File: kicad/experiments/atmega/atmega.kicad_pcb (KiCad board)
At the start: 2 copper layers, 8 parts, among them IC1 ATMEGA328P-A, P1 ISCP, P2 SERIAL, P3 CONN_01X05

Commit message: Layout
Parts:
- added C3: 0.1uF, Capacitors_SMD:C_0805_HandSoldering, F.Cu at (152.0, 94.7)
- added P4: GPIO, theapi:SMD_Header_Straight_1x05, B.Cu at (140.2, 106.2)
- added R2: 10k, Resistors_SMD:R_0805_HandSoldering, B.Cu at (142.8, 111.7)
- P2: value SERIAL -> FTDI; footprint Pin_Headers:Pin_Header_Straight_1x03 -> Socket_Strips:Socket_Strip_Straight_1x06
- P3: value CONN_01X05 -> I2C; footprint Pin_Headers:Pin_Header_Straight_1x05 -> SMD_Header_Straight_1x05; moved to B.Cu
- moved D1 75.0 mm to (142.2, 111.3), turned to 180 degrees
- moved C2 64.1 mm to (139.3, 96.6), turned to 90 degrees
- moved P3 63.2 mm to (152.0, 95.9), turned to 180 degrees
- moved P2 62.9 mm to (139.7, 92.5), turned to 0 degrees
- moved R1 61.3 mm to (142.7, 108.7)
- moved IC1 59.7 mm to (146.1, 101.6)
- moved C1 55.8 mm to (139.3, 101.7), turned to 270 degrees
- moved P1 45.8 mm to (152.4, 111.8), turned to 180 degrees
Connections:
- P1 pad 3: /CLK -> /SCK
- P2 pad 2: /TX -> GND
- P2 pad 3: /RX -> +3V3
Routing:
- net GND: track 0.00 -> 64.9 mm, vias 0 -> 1
- net +3V3: track 0.00 -> 57.8 mm, vias 0 -> 1
- net /RESET: track 0.00 -> 36.6 mm
- net /INT0: track 0.00 -> 13.9 mm, vias 0 -> 1
- net /SCK: track 0.00 -> 12.4 mm, vias 0 -> 1
- net /PD6: track 0.00 -> 10.9 mm, vias 0 -> 1
- net /PB2/SS: track 0.00 -> 8.99 mm, vias 0 -> 1
- net /SDA: track 0.00 -> 8.88 mm, vias 0 -> 1
- net /MISO: track 0.00 -> 8.74 mm
- net /SCL: track 0.00 -> 8.53 mm, vias 0 -> 1
- net /PB1: track 0.00 -> 8.19 mm, vias 0 -> 1
- net /PD5: track 0.00 -> 8.10 mm, vias 0 -> 1
- net /PD3: track 0.00 -> 7.92 mm, vias 0 -> 1
- net /RX: track 0.00 -> 7.92 mm
- net /TX: track 0.00 -> 6.72 mm
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- added copper zone on B.Cu, net GND
- added copper zone on F.Cu, net GND
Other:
- board outline added: 16.8 x 23.4 mm
- net class Default: clearance 0.1524 -> 0.2032; trace_width 0.1524 -> 0.2032
- rule trace_clearance: 0.1524 -> 0.2032
- rule trace_min: 0.1524 -> 0.2032

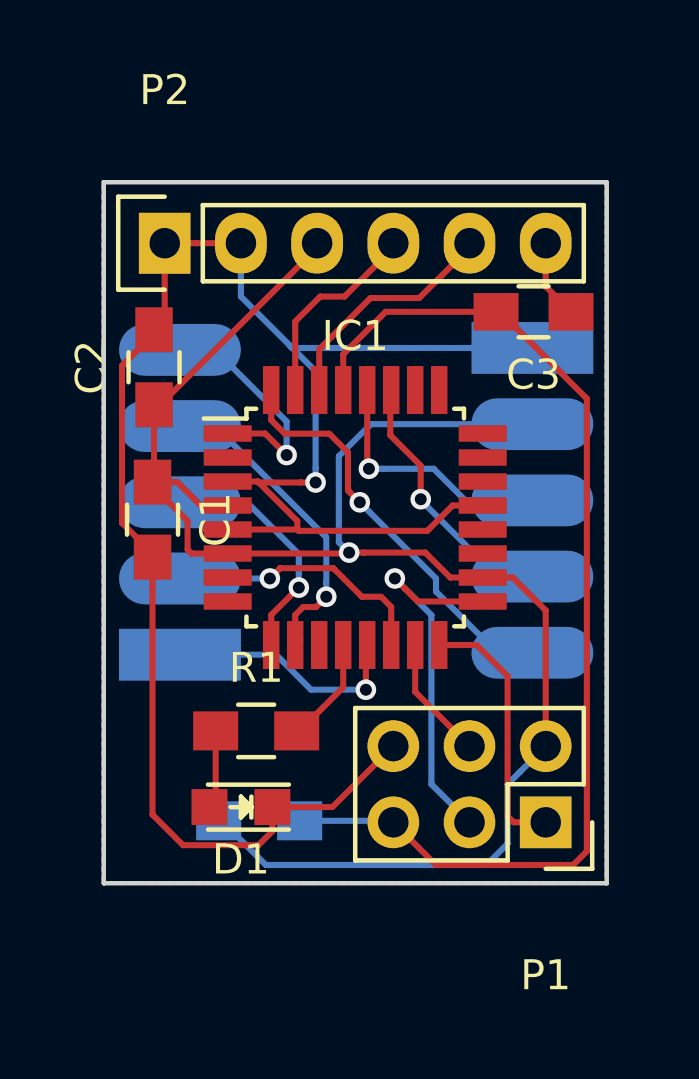
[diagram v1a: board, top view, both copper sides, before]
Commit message: Through hole headers
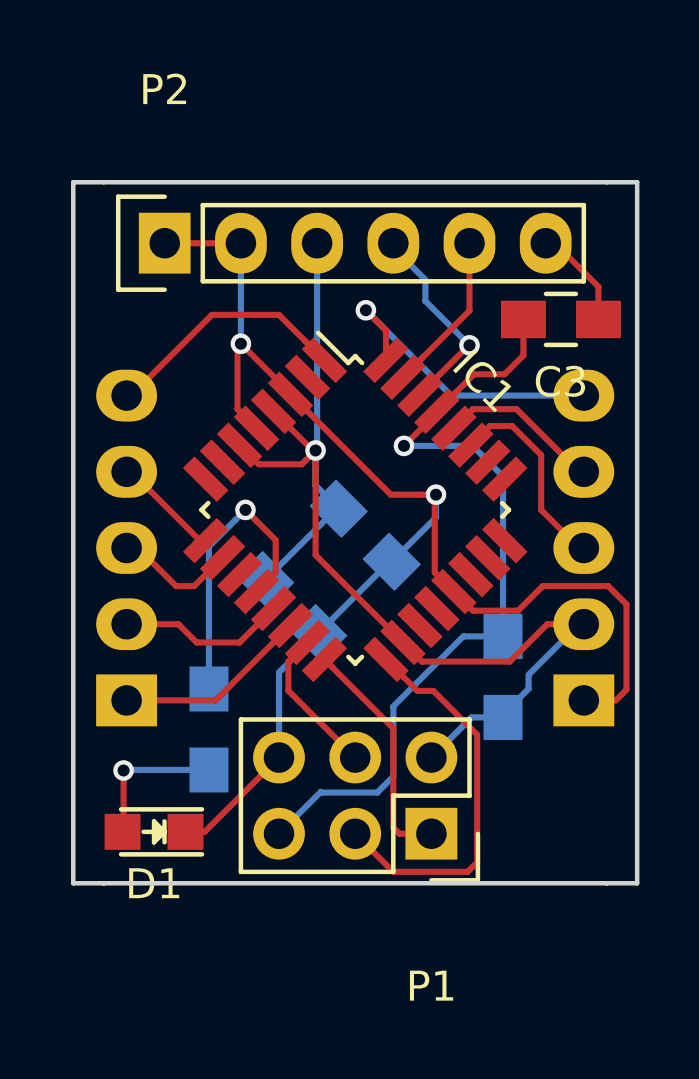
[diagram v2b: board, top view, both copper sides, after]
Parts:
- C1, C2, R1: moved to B.Cu
- P3: footprint SMD_Header_Straight_1x05 -> Pin_Headers:Pin_Header_Straight_1x05
- P4: footprint theapi:SMD_Header_Straight_1x05 -> Pin_Headers:Pin_Header_Straight_1x05
- moved P3 11.9 mm to (153.7, 107.7), turned to 0 degrees
- moved R2 9.44 mm to (151.0, 106.9), turned to 90 degrees
- moved C2 9.20 mm to (143.9, 104.6), turned to 315 degrees
- moved C1 7.11 mm to (146.4, 102.2), turned to 315 degrees
- moved P1 3.83 mm to (148.6, 112.1)
- moved D1 3.01 mm to (139.3, 112.1)
- moved P4 2.34 mm to (138.4, 107.7)
- moved R1 1.58 mm to (141.2, 108.7), turned to 90 degrees
- moved C3 0.95 mm to (152.9, 95.0)
- moved IC1 0.25 mm to (146.1, 101.3), turned to 315 degrees
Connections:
- P2 pad 4: /TX -> /RX
- P2 pad 5: /RX -> /TX
- P3 pad 3: /SCL -> /SDA
- P3 pad 4: /SDA -> /SCL
- P4 pad 1: /PB1 -> /PB2/SS
- P4 pad 2: /PB2/SS -> /PB1
- P4 pad 3: /PD5 -> /PD6
- P4 pad 4: /PD6 -> /PD5
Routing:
- net +3V3: track 57.8 -> 39.3 mm
- net GND: track 64.9 -> 47.8 mm, vias 1 -> 2
- net (no net): track 0.00 -> 15.2 mm
- net /RESET: track 36.6 -> 27.3 mm, vias 0 -> 1
- net /PD6: track 10.9 -> 4.12 mm, vias 1 -> 0
- net /PB0: track 3.56 -> 9.87 mm, vias 0 -> 1
- net /PD5: track 8.10 -> 3.59 mm, vias 1 -> 0
- net /INT0: track 13.9 -> 10.4 mm
- net /SCL: track 8.53 -> 5.46 mm, vias 1 -> 0
- net /PB2/SS: track 8.99 -> 6.50 mm, vias 1 -> 0
- net /PB1: track 8.19 -> 5.77 mm, vias 1 -> 0
- net Net-(D1-Pad2): track 2.63 -> 4.91 mm, vias 0 -> 1
- net /SDA: track 8.88 -> 6.78 mm, vias 1 -> 0
- net /TX: track 6.72 -> 5.54 mm
- net /RX: track 7.92 -> 6.94 mm, vias 0 -> 1
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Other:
- board size 16.8 x 23.4 mm -> 18.8 x 23.4 mm

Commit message: Silkscreen
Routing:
- net (no net): track 15.2 -> 0.00 mm
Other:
- board text added: "."
- board text added: "2"
- board text added: "3"
- board text added: "3V3"
- board text added: "5"
- board text added: "6"
- board text added: "9"
- board text added: "A4"
- board text added: "A5"
- board text added: "DTR"
- board text added: "GND"
- board text added: "RX"
- board text added: "TX"
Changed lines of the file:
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@@
     (area 136.576999 90.348999 155.523001 113.867001)
     (thickness 1.6)
-    (drawings 9)
-    (tracks 165)
+    (drawings 24)
+    (tracks 164)
     (zones 0)
     (modules 11)
@@
     (aux_axis_origin 0 0)
     (grid_origin 139.7 92.456)
-    (visible_elements 7FFFFFFF)
+    (visible_elements 7FFFFF7F)
     (pcbplotparams
       (layerselection 0x010f0_80000001)
@@
     (tags "capacitor 0805")
     (attr smd)
-    (fp_text reference C2 (at 0 2.1 315) (layer B.SilkS)
-      (effects (font (size 1 1) (thickness 0.15)) (justify mirror))
-    )
-    (fp_text value 10uF (at 0 -2.1 315) (layer B.Fab)
-      (effects (font (size 1 1) (thickness 0.15)) (justify mirror))
+    (fp_text reference C2 (at 0.007237 1.76013 315) (layer B.SilkS)
+      (effects (font (size 1.016 1.016) (thickness 0.1524)) (justify mirror))
+    )
+    (fp_text value 10uF (at 0 -2.1 315) (layer B.SilkS) hide
+      (effects (font (size 1.016 1.016) (thickness 0.1524)) (justify mirror))
     )
     (fp_line (start -2.3 1) (end 2.3 1) (layer B.CrtYd) (width 0.05))
@@
     (tags "QFP 0.8")
     (attr smd)
-    (fp_text reference IC1 (at 0 -6.05 315) (layer F.SilkS)
-      (effects (font (size 1 1) (thickness 0.15)))
-    )
-    (fp_text value ATMEGA328P-A (at 0 6.05 315) (layer F.Fab)
+    (fp_text reference IC1 (at 0 -6.05 315) (layer F.SilkS) hide
+      (effects (font (size 1 1) (thickness 0.15)))
+    )
+    (fp_text value ATMEGA328P-A (at 0 6.05 315) (layer F.Fab) hide
       (effects (font (size 1 1) (thickness 0.15)))
     )
@@
     (tags "capacitor 0805")
     (attr smd)
-    (fp_text reference C1 (at 0 2.1 315) (layer B.SilkS)
-      (effects (font (size 1 1) (thickness 0.15)) (justify mirror))
+    (fp_text reference C1 (at -0.007237 1.688288 315) (layer B.SilkS)
+      (effects (font (size 1.016 1.016) (thickness 0.1524)) (justify mirror))
     )
     (fp_text value 0.1uF (at 0 -2.1 315) (layer B.Fab)
@@
     (tags "LED 0805 SMD")
     (attr smd)
-    (fp_text reference D1 (at 0 -1.75 180) (layer F.SilkS)
-      (effects (font (size 1 1) (thickness 0.15)))
-    )
-    (fp_text value LED (at 0 1.75 180) (layer F.Fab)
+    (fp_text reference D1 (at 0 -1.75 180) (layer F.SilkS) hide
+      (effects (font (size 1 1) (thickness 0.15)))
+    )
+    (fp_text value LED (at 0 1.75 180) (layer F.Fab) hide
       (effects (font (size 1 1) (thickness 0.15)))
     )
@@
     (descr "Through hole socket strip")
     (tags "socket strip")
-    (fp_text reference P1 (at 0 -5.1 180) (layer F.SilkS)
-      (effects (font (size 1 1) (thickness 0.15)))
-    )
-    (fp_text value ISCP (at 0 -3.1 180) (layer F.Fab)
+    (fp_text reference P1 (at 0 -5.1 180) (layer F.SilkS) hide
+      (effects (font (size 1 1) (thickness 0.15)))
+    )
+    (fp_text value ISCP (at 0 -3.1 180) (layer F.Fab) hide
       (effects (font (size 1 1) (thickness 0.15)))
     )
@@
     (descr "Through hole socket strip")
     (tags "socket strip")
-    (fp_text reference P2 (at 0 -5.1) (layer F.SilkS)
+    (fp_text reference P2 (at 0 -5.1) (layer F.SilkS) hide
       (effects (font (size 1 1) (thickness 0.15)))
     )
@@
     (tags "capacitor 0805")
     (attr smd)
-    (fp_text reference C3 (at 0 -2.1 180) (layer F.SilkS)
-      (effects (font (size 1 1) (thickness 0.15)))
+    (fp_text reference C3 (at 1.9812 -1.778 180) (layer F.SilkS) hide
+      (effects (font (size 1.016 1.016) (thickness 0.127)))
     )
     (fp_text value 0.1uF (at 0 2.1 180) (layer F.Fab)
@@
     (descr "Through hole pin header")
     (tags "pin header")
-    (fp_text reference P3 (at 0 5.1) (layer B.SilkS)
+    (fp_text reference P3 (at 0 5.1) (layer B.SilkS) hide
       (effects (font (size 1 1) (thickness 0.15)) (justify mirror))
     )
@@
     (descr "Through hole pin header")
     (tags "pin header")
-    (fp_text reference P4 (at 0 5.1) (layer B.SilkS)
+    (fp_text reference P4 (at 0 5.1) (layer B.SilkS) hide
       (effects (font (size 1 1) (thickness 0.15)) (justify mirror))
     )
@@
     )
   )
+  (gr_text GND (at 151.13 107.5436) (layer F.SilkS)
+    (effects (font (size 1.016 1.016) (thickness 0.127)))
+  )
+  (gr_text 3V3 (at 151.1808 105.8672) (layer F.SilkS)
+    (effects (font (size 1.016 1.016) (thickness 0.127)))
+  )
+  (gr_text A4 (at 151.9428 103.886) (layer F.SilkS)
+    (effects (font (size 1.016 1.016) (thickness 0.127)))
+  )
+  (gr_text A5 (at 152.146 98.9076) (layer F.SilkS)
+    (effects (font (size 1.016 1.016) (thickness 0.127)))
+  )
+  (gr_text 2 (at 152.146 96.9772) (layer F.SilkS)
+    (effects (font (size 1.016 1.016) (thickness 0.127)))
+  )
+  (gr_text 9 (at 139.954 105.9688) (layer F.SilkS)
+    (effects (font (size 1.016 1.016) (thickness 0.127)))
+  )
+  (gr_text 6 (at 139.9032 103.7336) (layer F.SilkS)
+    (effects (font (size 1.016 1.016) (thickness 0.127)))
+  )
+  (gr_text 5 (at 140.0048 99.1616) (layer F.SilkS)
+    (effects (font (size 1.016 1.016) (thickness 0.127)))
+  )
+  (gr_text 3 (at 140.0556 96.774) (layer F.SilkS)
+    (effects (font (size 1.016 1.016) (thickness 0.127)))
+  )
+  (gr_text GND (at 141.1732 94.488) (layer F.SilkS)
+    (effects (font (size 1.016 1.016) (thickness 0.127)))
+  )
+  (gr_text 3V3 (at 144.7292 94.488) (layer F.SilkS)
+    (effects (font (size 1.016 1.016) (thickness 0.127)))
+  )
+  (gr_text DTR (at 154.4828 92.456 90) (layer F.SilkS)
+    (effects (font (size 1.016 1.016) (thickness 0.127)))
+  )
+  (gr_text TX (at 149.86 94.488) (layer F.SilkS)
+    (effects (font (size 1.016 1.016) (thickness 0.127)))
+  )
+  (gr_text RX (at 147.32 94.488) (layer F.SilkS)
+    (effects (font (size 1.016 1.016) (thickness 0.127)))
+  )
+  (gr_text . (at 145.5928 94.6912) (layer F.SilkS)
+    (effects (font (size 2.032 2.032) (thickness 0.381)))
+  )
   (gr_line (start 136.652 90.424) (end 137.668 90.424) (angle 90) (layer Edge.Cuts) (width 0.15))
   (gr_line (start 136.652 113.792) (end 136.652 90.424) (angle 90) (layer Edge.Cuts) (width 0.15))
@@
   (gr_line (start 154.432 113.792) (end 137.668 113.792) (angle 90) (layer Edge.Cuts) (width 0.15))
   (gr_line (start 137.668 90.424) (end 154.432 90.424) (angle 90) (layer Edge.Cuts) (width 0.15))
-  (segment (start 134.5184 101.6508) (end 149.7584 101.6508) (width 0.2032) (layer Cmts.User) (net 0))
   (segment (start 143.0528 103.6828) (end 145.430166 101.305434) (width 0.2032) (layer B.Cu) (net 1))
   (segment (start 145.430166 101.305434) (end 145.501434 101.305434) (width 0.2032) (layer B.Cu) (net 1))
